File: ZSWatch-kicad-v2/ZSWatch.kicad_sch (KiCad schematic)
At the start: 71 parts, among them IC1 ESDALC6V1W5, IC2 XC9265C181MR-G, IC3 TPS61023DRLT, IC4 MAX30101EFD+T, IC5 FAN5622SX, IC6 BMI270, IC7 LIS2MDLTR, J2 Charger and programming heade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, M1 Vibrator DC Motor, U1 MAX1811ESA+, U10 0_NORA-B106, U11 TXB0104QRUTRQ1/NTS0104GU12, U13 GC9A01A_CST816S, U2 DMC2400UV-7, U3 NCV300LSN36T1G, U4 BMP581, U5 BME688, U6 DRV2603RUNT, U7 XC9265A331MR-G

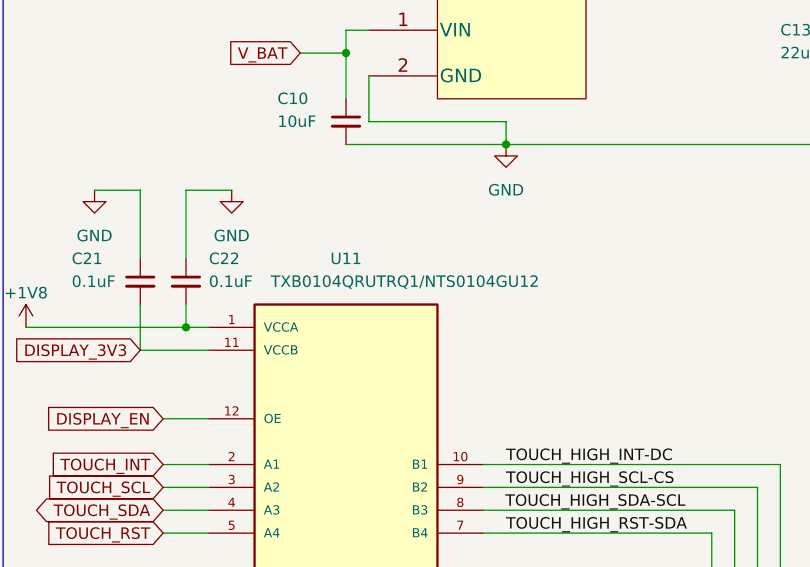
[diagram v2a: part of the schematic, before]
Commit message: Changed logic converter IC to NTS0104, no variant with old one. Re-generate ibom.
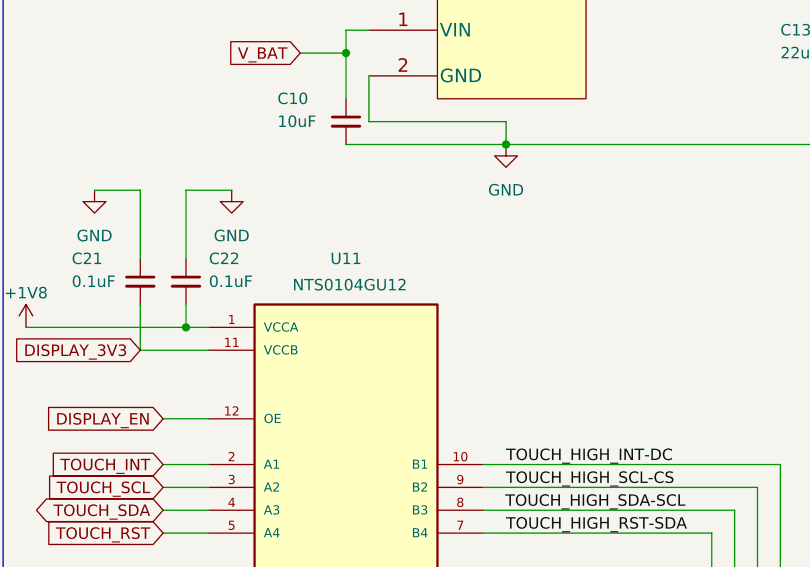
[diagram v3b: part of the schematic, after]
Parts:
- U11: value TXB0104QRUTRQ1/NTS0104GU12 -> NTS0104GU12; Alt buy https://www.digikey.se/en/products/detail/nxp-usa-inc/NTS01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 -> (none); Alt datasheet https://www.nxp.com/docs/en/data-sheet/NTS0104.pdf -> (none); Version for touch variant NTS0104GU12 -> (none); buy1 https://www.mouser.se/ProductDetail/Texas-Instruments/TXB01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 -> https://www.digikey.se/en/products/detail/nxp-usa-inc/NTS01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; buy2 https://www.arrow.com/en/products/txb0104qrutrq1/texas-inst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 -> (none); buy3 https://www.digikey.se/en/products/detail/TXB0104QRUTRQ1/29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 -> (none)
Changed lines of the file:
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@@
     (in_bom yes) (on_board yes)
     (property "Reference" "U11" (id 0) (at 274.32 223.52 0))
-    (property "Value" "TXB0104QRUTRQ1/NTS0104GU12" (id 1) (at 280.8735 226.0542 0))
+    (property "Value" "NTS0104GU12" (id 1) (at 274.7458 226.438 0))
     (property "Footprint" "SamacSys_Parts:HPA01164RUTR" (id 2) (at 274.32 246.38 0)
       (effects (font (size 1.27 1.27)) (justify left bottom) hide)
     )
-    (property "Datasheet" "https://www.ti.com/general/docs/suppproductinfo.tsp?distId=10&gotoUrl=https%3A%2F%2Fwww.ti.com%2Flit%2Fgpn%2Ftxb0104-q1" (id 3) (at 274.32 246.38 0)
+    (property "Datasheet" "https://www.nxp.com/docs/en/data-sheet/NTS0104.pdf" (id 3) (at 274.32 246.38 0)
       (effects (font (size 1.27 1.27)) (justify left bottom) hide)
     )
@@
       (effects (font (size 1.27 1.27)) (justify left bottom) hide)
     )
-    (property "buy1" "https://www.mouser.se/ProductDetail/Texas-Instruments/TXB0104QRUTRQ1?qs=%252B7BPNfeNhvXA8DYPWokk1A%3D%3D" (id 8) (at 274.32 246.38 0)
-      (effects (font (size 1.27 1.27)) hide)
-    )
-    (property "buy2" "https://www.arrow.com/en/products/txb0104qrutrq1/texas-instruments?region=nac&utm_campaign=octopart_2022&utm_content=inv_listing&utm_currency=USD&utm_keyword=TXB0104QRUTRQ1&utm_medium=aggregator&utm_source=octopart" (id 9) (at 274.32 246.38 0)
-      (effects (font (size 1.27 1.27)) hide)
-    )
-    (property "buy3" "https://www.digikey.se/en/products/detail/TXB0104QRUTRQ1/296-41033-1-ND/5178910?curr=usd&utm_campaign=buynow&utm_medium=aggregator&utm_source=octopart" (id 10) (at 274.32 246.38 0)
-      (effects (font (size 1.27 1.27)) hide)
-    )
-    (property "Version for touch variant" "NTS0104GU12" (id 11) (at 274.32 246.38 0)
-      (effects (font (size 1.27 1.27)) hide)
-    )
-    (property "Alt datasheet" "https://www.nxp.com/docs/en/data-sheet/NTS0104.pdf" (id 12) (at 274.32 246.38 0)
-      (effects (font (size 1.27 1.27)) hide)
-    )
-    (property "Alt buy" "https://www.digikey.se/en/products/detail/nxp-usa-inc/NTS0104GU12-115/2763907" (id 13) (at 274.32 246.38 0)
+    (property "buy1" "https://www.digikey.se/en/products/detail/nxp-usa-inc/NTS0104GU12-115/2763907" (id 8) (at 274.32 246.38 0)
       (effects (font (size 1.27 1.27)) hide)
     )
@@
     )
     (path "/19dfefc0-dc07-4bb3-8b08-909b7b408eba"
-      (reference "U11") (unit 1) (value "TXB0104QRUTRQ1/NTS0104GU12") (footprint "SamacSys_Parts:HPA01164RUTR")
+      (reference "U11") (unit 1) (value "NTS0104GU12") (footprint "SamacSys_Parts:HPA01164RUTR")
     )
     (path "/8bfefcd0-7370-479d-9a79-9bfe38630ab1"
